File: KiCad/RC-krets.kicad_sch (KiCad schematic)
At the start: 3 parts

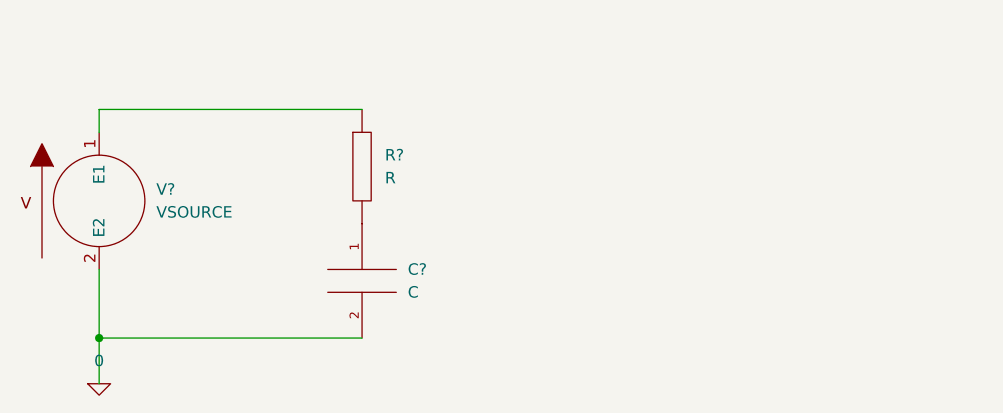
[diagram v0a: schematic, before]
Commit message: Mixtrade med RC-krets.kicad_sch
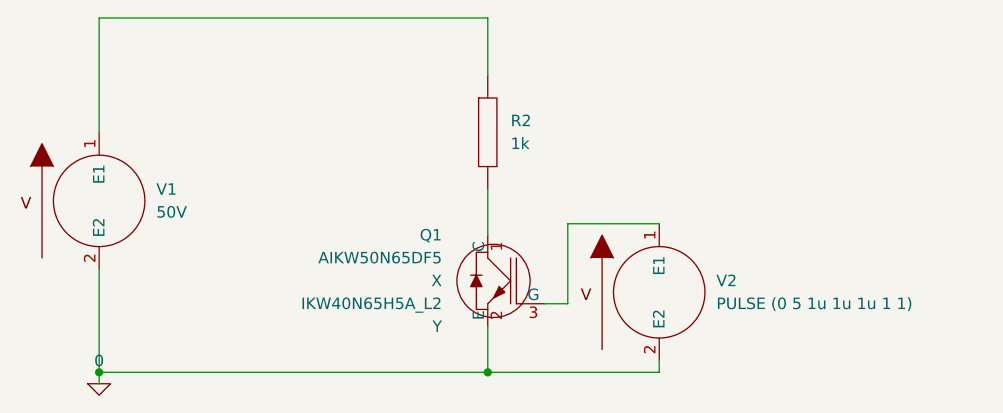
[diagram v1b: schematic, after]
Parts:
- removed C?: C, symbol pspice:C
- removed R?: R, symbol pspice:R
- added Q1: AIKW50N65DF5, symbol IGBT:AIKW50N65DF5
- added R2: 1k, symbol pspice:R
- added V2: PULSE (0 5 1u 1u 1u 1 1), symbol pspice:VSOURCE
- V1: renamed from V?; value VSOURCE -> 50V
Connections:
- net 0: now also Q1.2 (E), V2.2 (E2)
- net at V1.1 (E1): now also R2.1
- new net: Q1.1 (C), R2.2
- new net: Q1.3 (G), V2.1 (E1)
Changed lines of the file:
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@@
 (kicad_sch (version 20211123) (generator eeschema)
   (paper "A4")
-  (junction (at 125.73 124.46) (diameter 0) (color 0 0 0 0)
+  (junction (at 125.73 128.27) (diameter 0) (color 0 0 0 0)
   )
-  (wire (pts (xy 125.73 116.84) (xy 125.73 124.46))
+  (junction (at 168.91 128.27) (diameter 0) (color 0 0 0 0)
+  )
+  (wire (pts (xy 187.96 128.27) (xy 168.91 128.27))
     (stroke (width 0) (type default) (color 0 0 0 0))
   )
-  (wire (pts (xy 125.73 124.46) (xy 154.94 124.46))
+  (wire (pts (xy 187.96 111.76) (xy 177.8 111.76))
     (stroke (width 0) (type default) (color 0 0 0 0))
   )
-  (wire (pts (xy 125.73 99.06) (xy 125.73 101.6))
+  (wire (pts (xy 168.91 88.9) (xy 168.91 95.25))
     (stroke (width 0) (type default) (color 0 0 0 0))
   )
-  (wire (pts (xy 125.73 124.46) (xy 125.73 129.54))
+  (wire (pts (xy 177.8 111.76) (xy 177.8 120.65))
     (stroke (width 0) (type default) (color 0 0 0 0))
   )
-  (wire (pts (xy 154.94 99.06) (xy 125.73 99.06))
+  (wire (pts (xy 125.73 88.9) (xy 125.73 101.6))
+    (stroke (width 0) (type default) (color 0 0 0 0))
+  )
+  (wire (pts (xy 177.8 120.65) (xy 175.26 120.65))
+    (stroke (width 0) (type default) (color 0 0 0 0))
+  )
+  (wire (pts (xy 125.73 128.27) (xy 125.73 129.54))
+    (stroke (width 0) (type default) (color 0 0 0 0))
+  )
+  (wire (pts (xy 168.91 107.95) (xy 168.91 113.03))
+    (stroke (width 0) (type default) (color 0 0 0 0))
+  )
+  (wire (pts (xy 125.73 128.27) (xy 168.91 128.27))
+    (stroke (width 0) (type default) (color 0 0 0 0))
+  )
+  (wire (pts (xy 168.91 128.27) (xy 168.91 123.19))
+    (stroke (width 0) (type default) (color 0 0 0 0))
+  )
+  (wire (pts (xy 125.73 116.84) (xy 125.73 128.27))
+    (stroke (width 0) (type default) (color 0 0 0 0))
+  )
+  (wire (pts (xy 125.73 88.9) (xy 168.91 88.9))
+    (stroke (width 0) (type default) (color 0 0 0 0))
+  )
+  (wire (pts (xy 187.96 127) (xy 187.96 128.27))
     (stroke (width 0) (type default) (color 0 0 0 0))
   )
   (symbol (lib_id "pspice:0") (at 125.73 129.54 0) (unit 1)
     (in_bom yes) (on_board yes) (fields_autoplaced)
-    (property "Reference" "#GND?" (id 0) (at 125.73 132.08 0)
+    (property "Reference" "#GND0101" (id 0) (at 125.73 132.08 0)
       (effects (font (size 1.27 1.27)) hide)
     )
@@
     (pin "1")
   )
-  (symbol (lib_id "pspice:R") (at 154.94 105.41 0) (unit 1)
+  (symbol (lib_id "pspice:R") (at 168.91 101.6 0) (unit 1)
     (in_bom yes) (on_board yes) (fields_autoplaced)
-    (property "Reference" "R?" (id 0) (at 157.48 104.1399 0)
+    (property "Reference" "R2" (id 0) (at 171.45 100.3299 0)
       (effects (font (size 1.27 1.27)) (justify left))
     )
-    (property "Value" "R" (id 1) (at 157.48 106.6799 0)
+    (property "Value" "1k" (id 1) (at 171.45 102.8699 0)
       (effects (font (size 1.27 1.27)) (justify left))
     )
-    (property "Footprint" "" (id 2) (at 154.94 105.41 0)
+    (property "Footprint" "" (id 2) (at 168.91 101.6 0)
       (effects (font (size 1.27 1.27)) hide)
     )
-    (property "Datasheet" "~" (id 3) (at 154.94 105.41 0)
-      (effects (font (size 1.27 1.27)) hide)
-    )
-    (pin "1")
-    (pin "2")
-  )
-  (symbol (lib_id "pspice:C") (at 154.94 118.11 0) (unit 1)
-    (in_bom yes) (on_board yes) (fields_autoplaced)
-    (property "Reference" "C?" (id 0) (at 160.02 116.8399 0)
-      (effects (font (size 1.27 1.27)) (justify left))
-    )
-    (property "Value" "C" (id 1) (at 160.02 119.3799 0)
-      (effects (font (size 1.27 1.27)) (justify left))
-    )
-    (property "Footprint" "" (id 2) (at 154.94 118.11 0)
-      (effects (font (size 1.27 1.27)) hide)
-    )
-    (property "Datasheet" "~" (id 3) (at 154.94 118.11 0)
+    (property "Datasheet" "~" (id 3) (at 168.91 101.6 0)
       (effects (font (size 1.27 1.27)) hide)
     )
@@
   (symbol (lib_id "pspice:VSOURCE") (at 125.73 109.22 0) (unit 1)
     (in_bom yes) (on_board yes) (fields_autoplaced)
-    (property "Reference" "V?" (id 0) (at 132.08 107.9499 0)
+    (property "Reference" "V1" (id 0) (at 132.08 107.9499 0)
       (effects (font (size 1.27 1.27)) (justify left))
     )
-    (property "Value" "VSOURCE" (id 1) (at 132.08 110.4899 0)
+    (property "Value" "50V" (id 1) (at 132.08 110.4899 0)
       (effects (font (size 1.27 1.27)) (justify left))
     )
@@
     (pin "2")
   )
+  (symbol (lib_id "pspice:VSOURCE") (at 187.96 119.38 0) (unit 1)
+    (in_bom yes) (on_board yes) (fields_autoplaced)
+    (property "Reference" "V2" (id 0) (at 194.31 118.1099 0)
+      (effects (font (size 1.27 1.27)) (justify left))
+    )
+    (property "Value" "PULSE (0 5 1u 1u 1u 1 1)" (id 1) (at 194.31 120.6499 0)
+      (effects (font (size 1.27 1.27)) (justify left))
+    )
+    (property "Footprint" "" (id 2) (at 187.96 119.38 0)
+      (effects (font (size 1.27 1.27)) hide)
+    )
+    (property "Datasheet" "~" (id 3) (at 187.96 119.38 0)
+      (effects (font (size 1.27 1.27)) hide)
+    )
+    (pin "1")
+    (pin "2")
+  )
+  (symbol (lib_id "IGBT:AIKW50N65DF5") (at 170.18 118.11 0) (mirror y) (unit 1)
+    (in_bom yes) (on_board yes) (fields_autoplaced)
+    (property "Reference" "Q1" (id 0) (at 163.83 113.0299 0)
+      (effects (font (size 1.27 1.27)) (justify left))
+    )
+    (property "Value" "AIKW50N65DF5" (id 1) (at 163.83 115.5699 0)
+      (effects (font (size 1.27 1.27)) (justify left))
+    )
+    (property "Footprint" "" (id 2) (at 170.18 118.11 0)
+      (effects (font (size 1.27 1.27)) hide)
+    )
+    (property "Datasheet" "" (id 3) (at 170.18 118.11 0)
+      (effects (font (size 1.27 1.27)) hide)
+    )
+    (property "Spice_Primitive" "X" (id 4) (at 163.83 118.1099 0)
+      (effects (font (size 1.27 1.27)) (justify left))
+    )
+    (property "Spice_Model" "IKW40N65H5A_L2" (id 5) (at 163.83 120.6499 0)
+      (effects (font (size 1.27 1.27)) (justify left))
+    )
+    (property "Spice_Netlist_Enabled" "Y" (id 6) (at 163.83 123.1899 0)
+      (effects (font (size 1.27 1.27)) (justify left))
+    )
+    (property "Spice_Lib_File" "${KIPRJMOD}\\..\\PySpice\\Libraries\\IGBT Discrete - 650V TRENCHSTOP 5 AUTO - H5.lib" (id 7) (at 163.83 124.4599 0)
+      (effects (font (size 1.27 1.27)) (justify left) hide)
+    )
+    (pin "1")
+    (pin "2")
+    (pin "3")
+  )
   (sheet_instances
     (path "/" (page "1"))
@@
   (symbol_instances
     (path "/3019cd7d-d905-4256-ac07-1e58a26f3c06"
-      (reference "#GND?") (unit 1) (value "0") (footprint "")
+      (reference "#GND0101") (unit 1) (value "0") (footprint "")
     )
-    (path "/961e37cd-505c-40aa-baef-0a680d665d8f"
-      (reference "C?") (unit 1) (value "C") (footprint "")
+    (path "/d605dd99-2afa-4862-ad86-bb1825478583"
+      (reference "Q1") (unit 1) (value "AIKW50N65DF5") (footprint "")
     )
-    (path "/7243eb0d-2759-4180-82f4-00ea24b88636"
-      (reference "R?") (unit 1) (value "R") (footprint "")
+    (path "/8096b25b-c4f0-4acf-8d87-698e00a66150"
+      (reference "R2") (unit 1) (value "1k") (footprint "")
     )
     (path "/ab8b0540-9c9f-4195-88f5-7bed0b0a8ed6"
-      (reference "V?") (unit 1) (value "VSOURCE") (footprint "")
+      (reference "V1") (unit 1) (value "50V") (footprint "")
+    )
+    (path "/d5d24a3f-c627-4f85-9b18-7d59863507c3"
+      (reference "V2") (unit 1) (value "PULSE (0 5 1u 1u 1u 1 1)") (footprint "")
     )
   )
